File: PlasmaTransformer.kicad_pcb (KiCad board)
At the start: 2 copper layers, 90 x 90 mm, 38 parts, among them J1 Barrel_Jack_MountingPin, J10 Screw_Terminal_01x01, J11 Screw_Terminal_01x01, J12 Screw_Terminal_01x01, J2 Conn_01x02_Pin, J3 Conn_Coaxial, J5 Conn_Coaxial, J6 Screw_Terminal_01x01, J7 Screw_Terminal_01x01, J8 AudioJack3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

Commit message: layout complete, commit before resync
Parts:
- moved R9 9.63 mm to (81.0, 81.4)
- moved R5 6.59 mm to (88.0, 81.4)
- moved R6 2.75 mm to (84.5, 83.2), turned to -90 degrees
- moved JP1 2.05 mm to (71.5, 102.2)
- moved C3 1.75 mm to (71.5, 94.2)
- moved R7 1.41 mm to (66.5, 92.0)
- moved C4 1.20 mm to (77.0, 94.2)
- moved JP2 1.20 mm to (77.0, 102.2)
- moved C5 0.65 mm to (82.5, 94.2)
- moved D2 0.50 mm to (100.0, 106.5)
- moved J3 0.50 mm to (59.5, 92.0)
- moved J5 0.50 mm to (59.5, 78.0)
- moved JP4 0.50 mm to (88.0, 102.2)
- moved JP3 0.35 mm to (82.5, 102.2)
- moved C6 0.10 mm to (88.0, 94.2)
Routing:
- net GND: track 0.00 -> 338.1 mm, vias 0 -> 6
- net Net-(J10-Pin_1): track 0.00 -> 128.8 mm, vias 0 -> 1
- net Net-(J2-Pin_1): track 0.00 -> 79.8 mm
- net Net-(J7-Pin_1): track 0.00 -> 61.0 mm
- net Net-(J12-Pin_1): track 0.00 -> 52.9 mm
- net Net-(D2-A2): track 0.00 -> 52.1 mm
- net Net-(R5-Pad1): track 0.00 -> 33.9 mm
- net Net-(J8-PadT): track 0.00 -> 16.3 mm
- net Net-(SW1-A): track 0.00 -> 14.1 mm
- net Net-(J5-In): track 0.00 -> 7.62 mm
- net Net-(J3-In): track 0.00 -> 6.09 mm
- net Net-(JP4-A): track 0.00 -> 5.95 mm
- net Net-(JP3-A): track 0.00 -> 5.95 mm
- net Net-(JP2-A): track 0.00 -> 5.95 mm
- net Net-(JP1-A): track 0.00 -> 5.95 mm
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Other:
- board text added: "-STORAGE INDUCTOR-"
- board text added: "15-24V"
- board text added: "DRAIN"
- board text added: "FAN"
- board text added: "GATE"
- board text added: "PLASMA COIL"
- board text added: "RESONANT CAPACITOR"

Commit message: final edits, silkscreens, generate Rev 1 manufacturing files
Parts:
- added D3: LED, LED_SMD:LED_1206_3216Metric, F.Cu at (115.1, 114.0)
- added L1: PCB Coil, Library:FEEDBACK_COIL_B, F.Cu at (115.0, 112.0)
- added R1: 1k, Resistor_SMD:R_1812_4532Metric, F.Cu at (125.0, 124.5)
- added R10: 1k, Resistor_SMD:R_1812_4532Metric, F.Cu at (118.0, 124.5)
- added R11: 1k, Resistor_SMD:R_1812_4532Metric, F.Cu at (111.0, 124.5)
- added R12: 1k, Resistor_SMD:R_1812_4532Metric, F.Cu at (104.0, 124.5)
- added R13: 680, Resistor_SMD:R_0805_2012Metric, F.Cu at (115.0, 110.2)
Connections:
- H1 pad 1: Net-(J12-Pin_1) -> Net-(J7-Pin_1)
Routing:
- net Net-(J7-Pin_1): track 61.0 -> 87.6 mm
- net Net-(J12-Pin_1): track 52.9 -> 33.3 mm
- net Net-(D3-K): track 0.00 -> 9.12 mm, vias 0 -> 2
- net Net-(J10-Pin_1): track 128.8 -> 137.4 mm
- net GND: track 338.1 -> 345.4 mm
- net Net-(D3-A): track 0.00 -> 3.96 mm
- net Net-(L1-Pad2): track 0.00 -> 3.39 mm
- net Net-(R11-Pad2): track 0.00 -> 2.72 mm
- net Net-(R10-Pad2): track 0.00 -> 2.72 mm
- net Net-(R1-Pad2): track 0.00 -> 2.72 mm
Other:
- board text added: "FEEDBACK SENSOR DESIGN BY SKY-GUIDED"
- board text added: "INDUCTIVELY-COUPLED PLASMA DRIVER"
- board text added: "REV 1 | APR 2025 | E. CHIU"

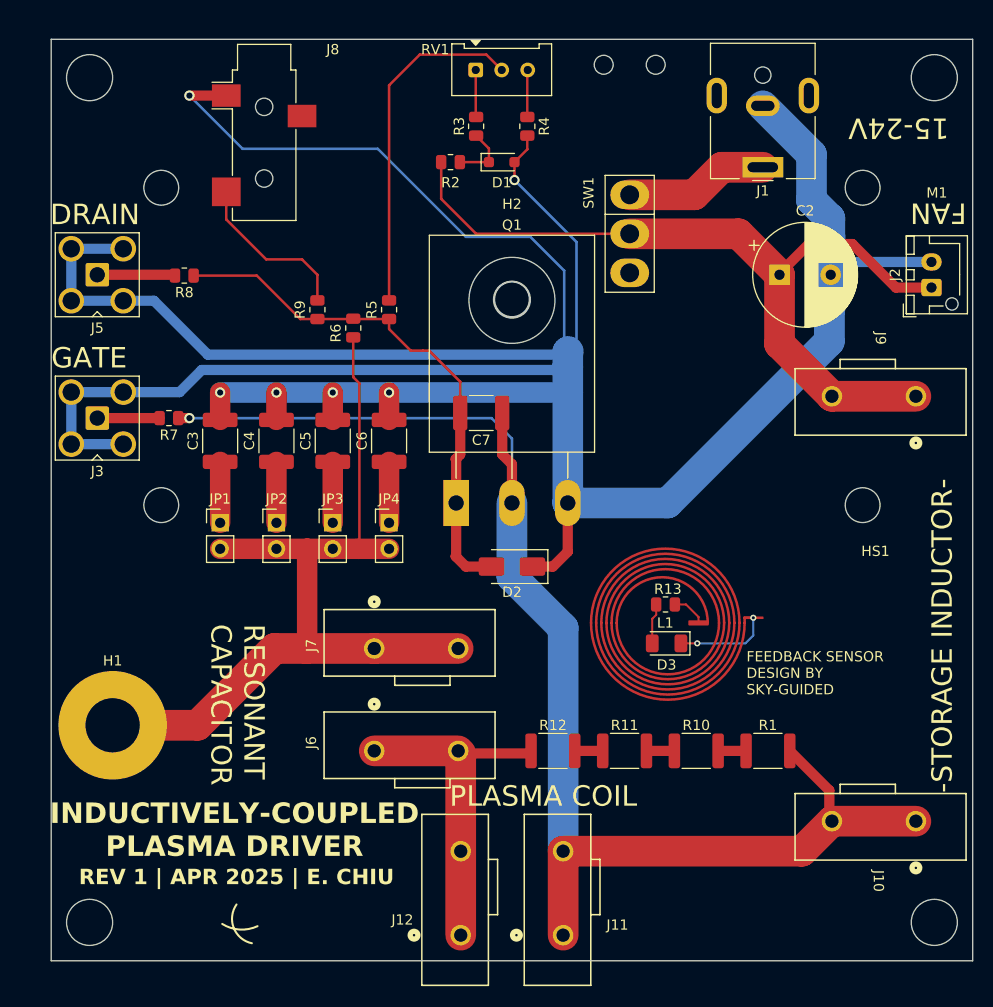
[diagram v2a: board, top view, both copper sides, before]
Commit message: Updated rev 2 design and manufacturing files.  Note BOM is not up to date.
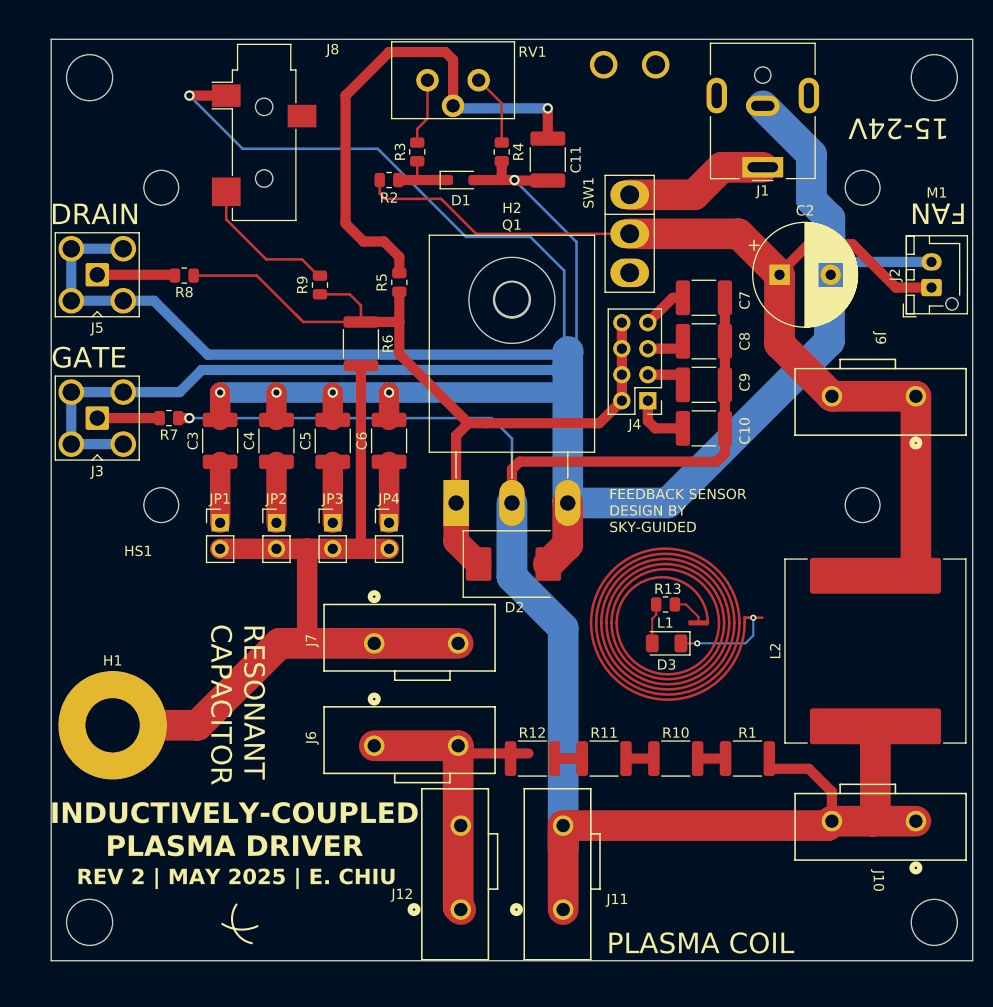
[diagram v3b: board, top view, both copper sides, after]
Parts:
- added C10: 220pF, Capacitor_SMD:C_1812_4532Metric, F.Cu at (118.8, 93.0)
- added C11: 1nF, Capacitor_SMD:C_1812_4532Metric, F.Cu at (103.5, 66.8)
- added C8: 220pF, Capacitor_SMD:C_1812_4532Metric, F.Cu at (118.8, 84.5)
- added C9: 220pF, Capacitor_SMD:C_1812_4532Metric, F.Cu at (118.8, 88.8)
- added J4: Conn_02x04_Odd_Even, Connector_PinHeader_2.54mm:PinHeader_2x04_P2.54mm_Vertical, F.Cu at (113.3, 90.3)
- added L2: L, Inductor_SMD:L_APV_APH1770, F.Cu at (135.5, 114.8)
- D2: footprint Diode_SMD:D_SMA -> Diode_SMD:D_SMC
- R1, R10, R11, R12: value 1k -> 100k
- R4: value 1.8k -> 1k
- R6: footprint Resistor_SMD:R_0805_2012Metric -> Resistor_SMD:R_1812_4532Metric
- R7, R8, R9: value 50 -> 49.9
- RV1: footprint Potentiometer_THT:Potentiometer_Bourns_3386W_Horizontal -> Library:SMC10H04-102A2020MTA
- moved C7 24.5 mm to (118.8, 80.2), turned to 0 degrees
- moved R3 6.27 mm to (90.8, 66.0)
- moved R2 6.25 mm to (88.0, 68.8)
- moved D1 4.37 mm to (95.0, 68.8)
- moved R4 3.54 mm to (99.0, 66.0)
- moved R5 2.84 mm to (89.0, 78.8)
- moved J11 2.50 mm to (105.0, 140.0)
- moved J12 2.50 mm to (95.0, 140.0)
- moved RV1 2.43 mm to (94.2, 59.0)
- moved R9 2.43 mm to (81.2, 79.0)
- moved R1 2.14 mm to (123.0, 125.2)
- moved R10 2.14 mm to (116.0, 125.2)
- moved R11 2.14 mm to (109.0, 125.2)
- moved R12 2.14 mm to (102.0, 125.2)
- moved R6 1.72 mm to (85.2, 84.8)
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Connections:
- C7 pad 1: Net-(J10-Pin_1) -> Net-(J4-Pin_7)
- C7 pad 2: Net-(D2-A2) -> Net-(J10-Pin_1)
- D2 pad 1: GND -> Net-(D2-K)
- D2 pad 2: Net-(D2-A2) -> GND
- Q1 pad 1: Net-(D2-A2) -> Net-(D2-K)
- R5 pad 2: Net-(D2-A2) -> Net-(D2-K)
- R6 pad 1: Net-(D2-A2) -> Net-(D2-K)
- R8 pad 1: Net-(D2-A2) -> Net-(D2-K)
- R9 pad 2: Net-(D2-A2) -> Net-(D2-K)
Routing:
- net Net-(D2-K): track 0.00 -> 83.0 mm
- net Net-(D2-A2): track 52.1 -> 0.00 mm
- net Net-(J10-Pin_1): track 137.4 -> 178.2 mm
- net Net-(J2-Pin_1): track 79.8 -> 101.2 mm
- net Net-(C11-Pad2): track 33.9 -> 50.1 mm, vias 0 -> 1
- net Net-(J4-Pin_1): track 0.00 -> 5.70 mm
- net Net-(J4-Pin_3): track 0.00 -> 4.47 mm
- net Net-(J4-Pin_7): track 0.00 -> 4.43 mm
- net Net-(J4-Pin_5): track 0.00 -> 2.70 mm
- net Net-(J8-PadT): track 16.3 -> 13.8 mm
- net Net-(R4-Pad1): track 4.60 -> 7.02 mm
- net Net-(J12-Pin_1): track 33.3 -> 30.9 mm
- net GND: track 345.4 -> 347.5 mm
- net Net-(R3-Pad2): track 4.60 -> 6.50 mm
- net Net-(J7-Pin_1): track 87.6 -> 89.1 mm
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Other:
- board text added: "REV 2 | MAY 2025 | E. CHIU"
- board text removed: "-STORAGE INDUCTOR-"
- board text removed: "REV 1 | APR 2025 | E. CHIU"

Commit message: modifying recommended values for successful 20cm toroid halo
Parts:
- C4, C5, C6: value 2.7nF -> 1.8nF
- D1: value D_Zener -> 10V
- D2: value SMAJ15CA -> 5.0SMDJ15CA; footprint Diode_SMD:D_SMC -> Diode_SMD:D_SMA
- L2: value L -> 9.2uH

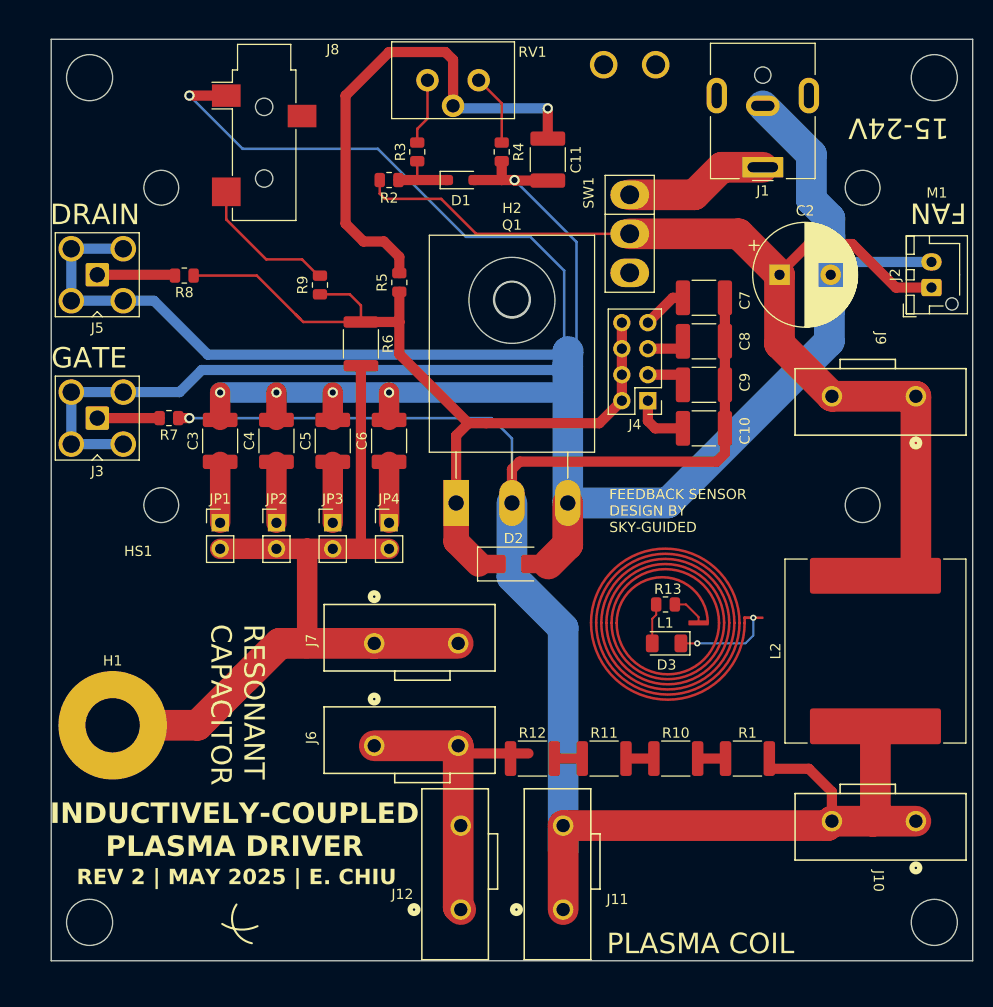
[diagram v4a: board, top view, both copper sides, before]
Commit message: rev 3 PCB adds auto ignite
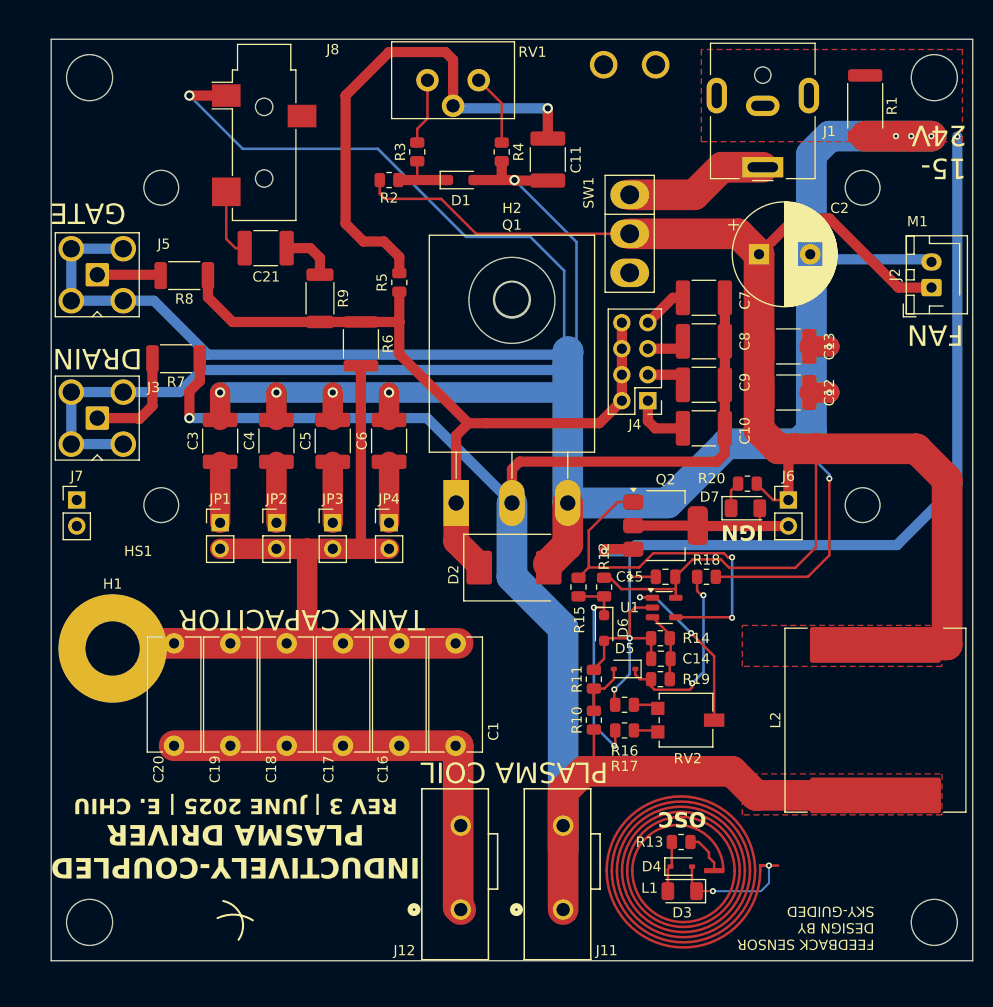
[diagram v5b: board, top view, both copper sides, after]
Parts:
- removed J10, J9: Screw_Terminal_01x01, Library:CONN_2604-3101_WAG
- added C1: 24pF, Capacitor_THT:C_Disc_D11.0mm_W5.0mm_P10.00mm, F.Cu at (94.5, 124.0)
- added C12: 1nF, Capacitor_SMD:C_1812_4532Metric, F.Cu at (127.0, 89.5)
- added C13: 100nF, Capacitor_SMD:C_1812_4532Metric, F.Cu at (127.0, 85.0)
- added C14: 22uF, Capacitor_SMD:C_0805_2012Metric, F.Cu at (114.5, 115.5)
- added C15: 100nF, Capacitor_SMD:C_0805_2012Metric, F.Cu at (115.0, 107.5)
- added C16: 24pF, Capacitor_THT:C_Disc_D11.0mm_W5.0mm_P10.00mm, F.Cu at (89.0, 124.0)
- added C17: 24pF, Capacitor_THT:C_Disc_D11.0mm_W5.0mm_P10.00mm, F.Cu at (83.5, 124.0)
- added C18: 24pF, Capacitor_THT:C_Disc_D11.0mm_W5.0mm_P10.00mm, F.Cu at (78.0, 124.0)
- added C19: 24pF, Capacitor_THT:C_Disc_D11.0mm_W5.0mm_P10.00mm, F.Cu at (72.5, 124.0)
- added C20: 24pF, Capacitor_THT:C_Disc_D11.0mm_W5.0mm_P10.00mm, F.Cu at (67.0, 124.0)
- added C21: 1nF, Capacitor_SMD:C_1812_4532Metric, F.Cu at (76.0, 75.4)
- added D4: D, Diode_SMD:D_SOD-323, F.Cu at (116.5, 135.8)
- added D5: D, Diode_SMD:D_SOD-323, F.Cu at (111.0, 116.5)
- added D6: 10V, Diode_SMD:D_SOD-323_HandSoldering, F.Cu at (109.0, 112.5)
- added D7: GREEN, LED_SMD:LED_1206_3216Metric, F.Cu at (122.8, 100.8)
- added Q2: BUK9832-55A, Package_TO_SOT_SMD:SOT-223-3_TabPin2, F.Cu at (115.0, 102.5)
- added R14: 22k, Resistor_SMD:R_0805_2012Metric, F.Cu at (114.5, 113.5)
- added R15: 4.7k, Resistor_SMD:R_0805_2012Metric, F.Cu at (106.5, 108.5)
- added R16: 0, Resistor_SMD:R_0805_2012Metric, F.Cu at (111.0, 120.0)
- added R17: 1k, Resistor_SMD:R_0805_2012Metric, F.Cu at (111.0, 122.5)
- added R18: 0, Resistor_SMD:R_0805_2012Metric, F.Cu at (119.0, 107.5)
- added R19: 22k, Resistor_SMD:R_0805_2012Metric, F.Cu at (114.5, 117.5)
- added R20: 4.7k, Resistor_SMD:R_0805_2012Metric, F.Cu at (123.0, 98.4)
- added RV2: 5k, Potentiometer_SMD:Potentiometer_Vishay_TS53YL_Vertical, F.Cu at (117.0, 121.5)
- added U1: LM397, Package_TO_SOT_SMD:SOT-23-5, F.Cu at (114.9, 110.5)
- D2: footprint Diode_SMD:D_SMA -> Diode_SMD:D_SMC
- D3: value LED -> AMBER
- J6, J7: value Screw_Terminal_01x01 -> Conn_01x02_Pin; footprint Library:CONN_2604-3101_WAG -> Connector_PinHeader_2.54mm:PinHeader_1x02_P2.54mm_Vertical
- R1: value 100k -> 0.05; footprint Resistor_SMD:R_1812_4532Metric -> Resistor_SMD:R_2512_6332Metric
- R10: value 100k -> 22k; footprint Resistor_SMD:R_1812_4532Metric -> Resistor_SMD:R_0805_2012Metric
- R11, R12: value 100k -> 1k; footprint Resistor_SMD:R_1812_4532Metric -> Resistor_SMD:R_0805_2012Metric
- R7, R8, R9: footprint Resistor_SMD:R_0805_2012Metric -> Resistor_SMD:R_2010_5025Metric
- moved R1 64.8 mm to (134.5, 61.5), turned to -90 degrees
- moved J6 47.0 mm to (127.0, 100.0), turned to 0 degrees
- moved J7 32.2 mm to (57.5, 100.0), turned to 0 degrees
- moved D3 24.2 mm to (116.6, 138.2)
- moved L1 24.2 mm to (116.5, 136.2)
- moved R13 23.3 mm to (116.5, 133.4)
- moved R12 18.2 mm to (109.0, 108.5), turned to 90 degrees
- moved R10 8.84 mm to (108.0, 121.5), turned to 90 degrees
- moved R11 7.81 mm to (108.0, 117.5), turned to 90 degrees
- moved H1 7.50 mm to (61.0, 114.5)
- moved L2 6.75 mm to (135.5, 121.5)
- moved R7 5.84 mm to (67.2, 86.2)
- moved C2 2.83 mm to (124.1, 76.0)
- moved R9 1.30 mm to (81.2, 80.3)
- moved D2 0.35 mm to (100.2, 106.6)
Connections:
- net Net-(D2-A1) renamed /GATE
- C10 pad 2: Net-(J10-Pin_1) -> /DRAIN
- C7 pad 2: Net-(J10-Pin_1) -> /DRAIN
- C8 pad 2: Net-(J10-Pin_1) -> /DRAIN
- C9 pad 2: Net-(J10-Pin_1) -> /DRAIN
- H1 pad 1: Net-(J7-Pin_1) -> Net-(JP1-B)
- J1 pad 2: GND -> /GND-IN
- J11 pad 1: Net-(J10-Pin_1) -> /DRAIN
- J6 pad 1: Net-(J12-Pin_1) -> Net-(J2-Pin_1)
- J7 pad 1: Net-(J7-Pin_1) -> unconnected-(J7-Pin_1-Pad1)
- J8 pad T: Net-(J8-PadT) -> Net-(C21-Pad2)
- JP1 pad 2: Net-(J7-Pin_1) -> Net-(JP1-B)
- JP2 pad 2: Net-(J7-Pin_1) -> Net-(JP1-B)
- JP3 pad 2: Net-(J7-Pin_1) -> Net-(JP1-B)
- JP4 pad 2: Net-(J7-Pin_1) -> Net-(JP1-B)
- L2 pad 2: Net-(J10-Pin_1) -> /DRAIN
- Q1 pad 2: Net-(J10-Pin_1) -> /DRAIN
- R1 pad 1: Net-(J10-Pin_1) -> /GND-IN
- R1 pad 2: Net-(R1-Pad2) -> GND
- R10 pad 1: Net-(R1-Pad2) -> /DRAIN
- R11 pad 2: Net-(R11-Pad2) -> /GND-IN
- R12 pad 1: Net-(R11-Pad2) -> Net-(D6-K)
- R12 pad 2: Net-(J12-Pin_1) -> Net-(J2-Pin_1)
- R6 pad 2: Net-(J7-Pin_1) -> Net-(JP1-B)
- R7 pad 1: Net-(J10-Pin_1) -> /DRAIN
- R9 pad 1: Net-(J8-PadT) -> Net-(C21-Pad1)
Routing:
- net Net-(J10-Pin_1): track 178.2 -> 0.00 mm, vias 1 -> 0
- net /DRAIN: track 0.00 -> 165.5 mm, vias 0 -> 1
- net /GND-IN: track 0.00 -> 107.2 mm, vias 0 -> 5
- net Net-(J7-Pin_1): track 89.1 -> 0.00 mm
- net Net-(JP1-B): track 0.00 -> 78.4 mm
- net Net-(J2-Pin_1): track 101.2 -> 166.4 mm
- net GND: track 347.5 -> 388.6 mm, vias 6 -> 12
- net Net-(Q2-G): track 0.00 -> 36.7 mm, vias 0 -> 2
- net Net-(D6-K): track 0.00 -> 21.2 mm, vias 0 -> 2
- net Net-(D5-K): track 0.00 -> 18.8 mm, vias 0 -> 2
- net Net-(U1--): track 0.00 -> 17.1 mm, vias 0 -> 2
- net Net-(D7-A): track 0.00 -> 16.9 mm
- net Net-(J8-PadT): track 13.8 -> 0.00 mm
- net Net-(J12-Pin_1): track 30.9 -> 43.9 mm
- net /GATE: track 83.0 -> 76.1 mm
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- added copper zone on F.Cu, net /DRAIN
- added copper zone on F.Cu, net /GND-IN
- added copper zone on F.Cu, net Net-(J2-Pin_1)
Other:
- board text added: "15- 24V"
- board text added: "IGN"
- board text added: "OSC"
- board text added: "REV 3 | JUNE 2025 | E. CHIU"
- board text added: "TANK CAPACITOR"
- board text removed: "15-24V"
- board text removed: "RESONANT CAPACITOR"
- board text removed: "REV 2 | MAY 2025 | E. CHIU"
